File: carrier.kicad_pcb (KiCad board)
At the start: 4 copper layers, 20.3 x 68.6 mm, 52 parts, among them J1 Conn_02x06_Odd_Even, J10 Conn_01x02, J11 Conn_01x02, J12 AudioJack3_SwitchTR, J2 Conn_01x26, J3 Conn_01x26, J4 TYPE-C-31-M-12, J5 Conn_01x02, J6 Conn_01x02, J7 Conn_01x02, J8 Conn_01x02, J9 Conn_01x02, U1 CARAVEL, U2 W25Q128JVS, U3 LP5907MFX-3.3, U4 LP5907MFX-1.8, U5 LP5907MFX-1.8, U6 LP5907MFX-3.3, U7 TPD2E001DRSR, U8 OPA340NA, U9 OPA340NA, X1 SG-5032CAN

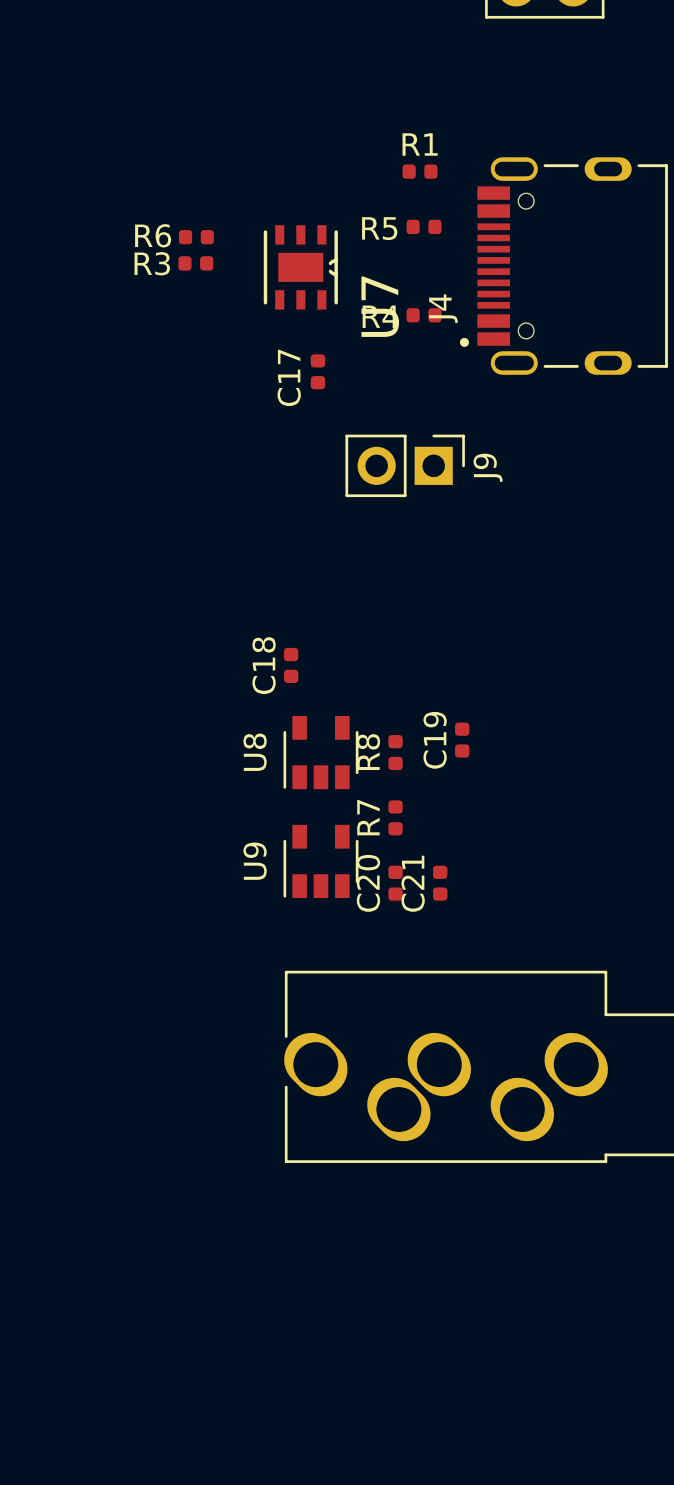
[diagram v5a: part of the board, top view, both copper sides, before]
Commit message: Add GND hook test point
Might want to add more test points for various things.
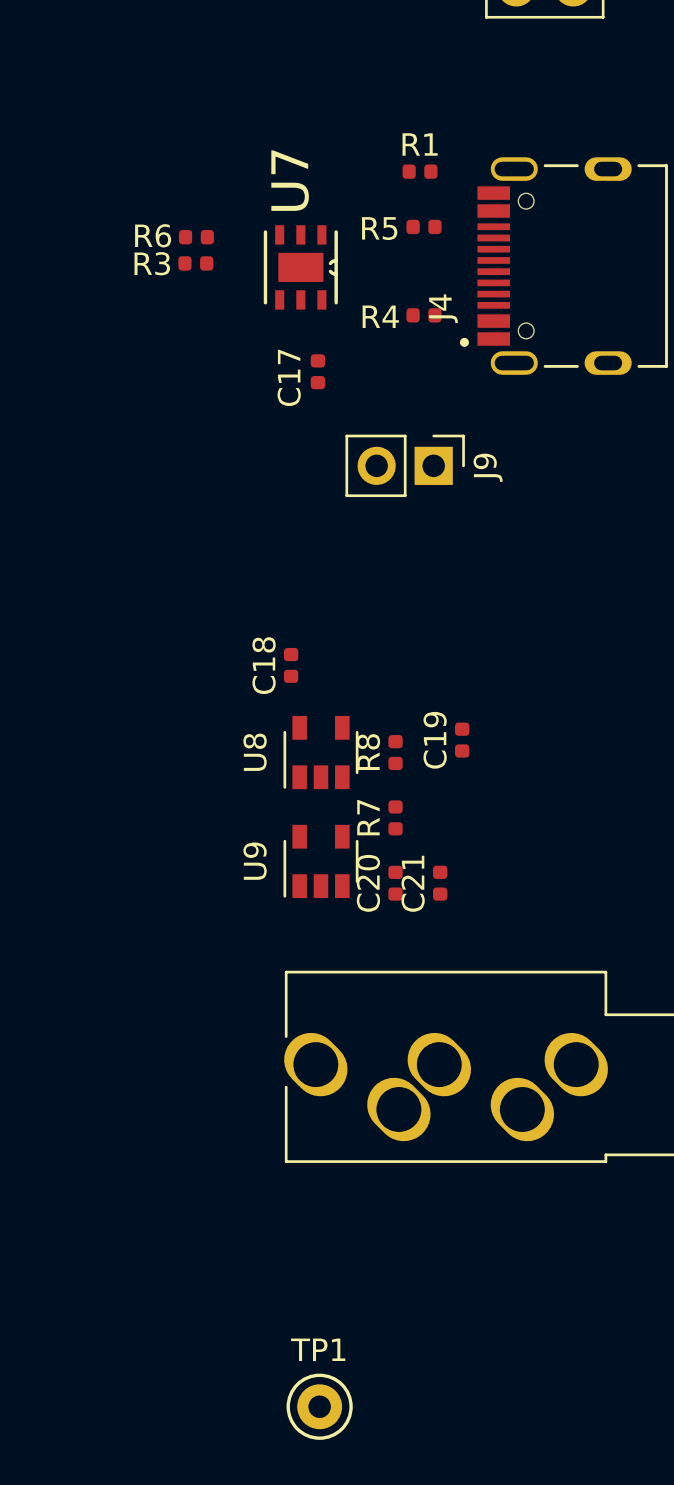
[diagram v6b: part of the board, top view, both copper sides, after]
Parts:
- added TP1: TestPoint, TestPoint:TestPoint_Keystone_5000-5004_Miniature, F.Cu at (114.3, 123.2)
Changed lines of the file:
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@@
     (property "Sheetname" "")
     (attr through_hole)
-    (fp_text reference "U7" (at 1.753155 -3.582515 -90) (layer "F.SilkS")
+    (fp_text reference "U7" (at -3.8608 0.4318 -90) (layer "F.SilkS")
       (effects (font (size 1.640512 1.640512) (thickness 0.015)))
     )
@@
       (net 89 "pcm_audio_2") (pintype "passive"))
     (model "${KISYS3DMOD}/Resistor_SMD.3dshapes/R_0402_1005Metric.wrl"
+      (offset (xyz 0 0 0))
+      (scale (xyz 1 1 1))
+      (rotate (xyz 0 0 0))
+    )
+  )
+  (footprint "TestPoint:TestPoint_Keystone_5000-5004_Miniature" (layer "F.Cu")
+    (at 114.3 123.19)
+    (descr "Keystone Miniature THM Test Point 5000-5004, http://www.keyelco.com/product-pdf.cfm?p=1309")
+    (tags "Through Hole Mount Test Points")
+    (property "Sheetfile" "carrier.kicad_sch")
+    (property "Sheetname" "")
+    (attr through_hole)
+    (fp_text reference "TP1" (at 0 -2.5) (layer "F.SilkS")
+      (effects (font (size 1 1) (thickness 0.15)))
+    )
+    (fp_text value "TestPoint" (at 0 2.5) (layer "F.Fab")
+      (effects (font (size 1 1) (thickness 0.15)))
+    )
+    (fp_text user "${REFERENCE}" (at 0 -2.5) (layer "F.Fab")
+      (effects (font (size 1 1) (thickness 0.15)))
+    )
+    (fp_circle (center 0 0) (end 1.4 0) (layer "F.SilkS") (width 0.15) (fill none))
+    (fp_circle (center 0 0) (end 1.65 0) (layer "F.CrtYd") (width 0.05) (fill none))
+    (fp_line (start -0.75 0.25) (end -0.75 -0.25) (layer "F.Fab") (width 0.15))
+    (fp_line (start 0.75 -0.25) (end 0.75 0.25) (layer "F.Fab") (width 0.15))
+    (fp_line (start -0.75 -0.25) (end 0.75 -0.25) (layer "F.Fab") (width 0.15))
+    (fp_line (start 0.75 0.25) (end -0.75 0.25) (layer "F.Fab") (width 0.15))
+    (fp_circle (center 0 0) (end 1.25 0) (layer "F.Fab") (width 0.15) (fill none))
+    (pad "1" thru_hole circle locked (at 0 0) (size 2 2) (drill 1) (layers *.Cu *.Mask)
+      (net 3 "GND") (pinfunction "1") (pintype "passive"))
+    (model "${KISYS3DMOD}/TestPoint.3dshapes/TestPoint_Keystone_5000-5004_Miniature.wrl"
       (offset (xyz 0 0 0))
       (scale (xyz 1 1 1))
@@
       (effects (font (size 1 1) (thickness 0.15)))
     )
+    (fp_line (start 4.47 2.6) (end -4.47 2.6) (layer "F.SilkS") (width 0.127))
+    (fp_line (start 4.47 1.37) (end 4.47 2.6) (layer "F.SilkS") (width 0.127))
+    (fp_line (start -4.47 -2.81) (end -4.47 -1.37) (layer "F.SilkS") (width 0.127))
     (fp_line (start -4.47 2.6) (end -4.47 1.37) (layer "F.SilkS") (width 0.127))
     (fp_line (start 4.47 -2.81) (end 4.47 -1.37) (layer "F.SilkS") (width 0.127))
-    (fp_line (start -4.47 -2.81) (end -4.47 -1.37) (layer "F.SilkS") (width 0.127))
-    (fp_line (start 4.47 1.37) (end 4.47 2.6) (layer "F.SilkS") (width 0.127))
-    (fp_line (start 4.47 2.6) (end -4.47 2.6) (layer "F.SilkS") (width 0.127))
     (fp_circle (center -3.4 -6.4) (end -3.3 -6.4) (layer "F.SilkS") (width 0.2) (fill none))
     (fp_line (start 5.095 2.85) (end 5.095 -6.07) (layer "F.CrtYd") (width 0.05))
     (fp_line (start -5.095 -6.07) (end -5.095 2.85) (layer "F.CrtYd") (width 0.05))
+    (fp_line (start -5.095 2.85) (end 5.095 2.85) (layer "F.CrtYd") (width 0.05))
     (fp_line (start 5.095 -6.07) (end -5.095 -6.07) (layer "F.CrtYd") (width 0.05))
-    (fp_line (start -5.095 2.85) (end 5.095 2.85) (layer "F.CrtYd") (width 0.05))
+    (fp_line (start -4.47 2.6) (end 4.47 2.6) (layer "F.Fab") (width 0.127))
     (fp_line (start 4.47 2.6) (end 4.47 -4.7) (layer "F.Fab") (width 0.127))
     (fp_line (start 4.47 -4.7) (end -4.47 -4.7) (layer "F.Fab") (width 0.127))
-    (fp_line (start -4.47 2.6) (end 4.47 2.6) (layer "F.Fab") (width 0.127))
     (fp_line (start -4.47 -4.7) (end -4.47 2.6) (layer "F.Fab") (width 0.127))
     (fp_circle (center -3.4 -6.4) (end -3.3 -6.4) (layer "F.Fab") (width 0.2) (fill none))
+    (pad "" np_thru_hole circle locked (at -2.89 -3.65 90) (size 0.7 0.7) (drill 0.7) (layers *.Cu *.Mask))
     (pad "" np_thru_hole circle locked (at 2.89 -3.65 90) (size 0.7 0.7) (drill 0.7) (layers *.Cu *.Mask))
-    (pad "" np_thru_hole circle locked (at -2.89 -3.65 90) (size 0.7 0.7) (drill 0.7) (layers *.Cu *.Mask))
     (pad "A1B12" smd rect locked (at -3.25 -5.095 90) (size 0.6 1.45) (layers "F.Cu" "F.Paste" "F.Mask")
       (net 3 "GND") (pinfunction "GND") (pintype "power_in"))
@@
     (fp_line (start -0.5 0.25) (end -0.5 -0.25) (layer "F.Fab") (width 0.1))
     (pad "1" smd roundrect locked (at -0.485 0 90) (size 0.59 0.64) (layers "F.Cu" "F.Paste" "F.Mask") (roundrect_rratio 0.25)
-      (net 82 "Net-(C19-Pad1)"))
+      (net 82 "Net-(C19-Pad1)") (pintype "passive"))
     (pad "2" smd roundrect locked (at 0.485 0 90) (size 0.59 0.64) (layers "F.Cu" "F.Paste" "F.Mask") (roundrect_rratio 0.25)
-      (net 3 "GND"))
+      (net 3 "GND") (pintype "passive"))
     (model "${KISYS3DMOD}/Capacitor_SMD.3dshapes/C_0402_1005Metric.wrl"
       (offset (xyz 0 0 0))

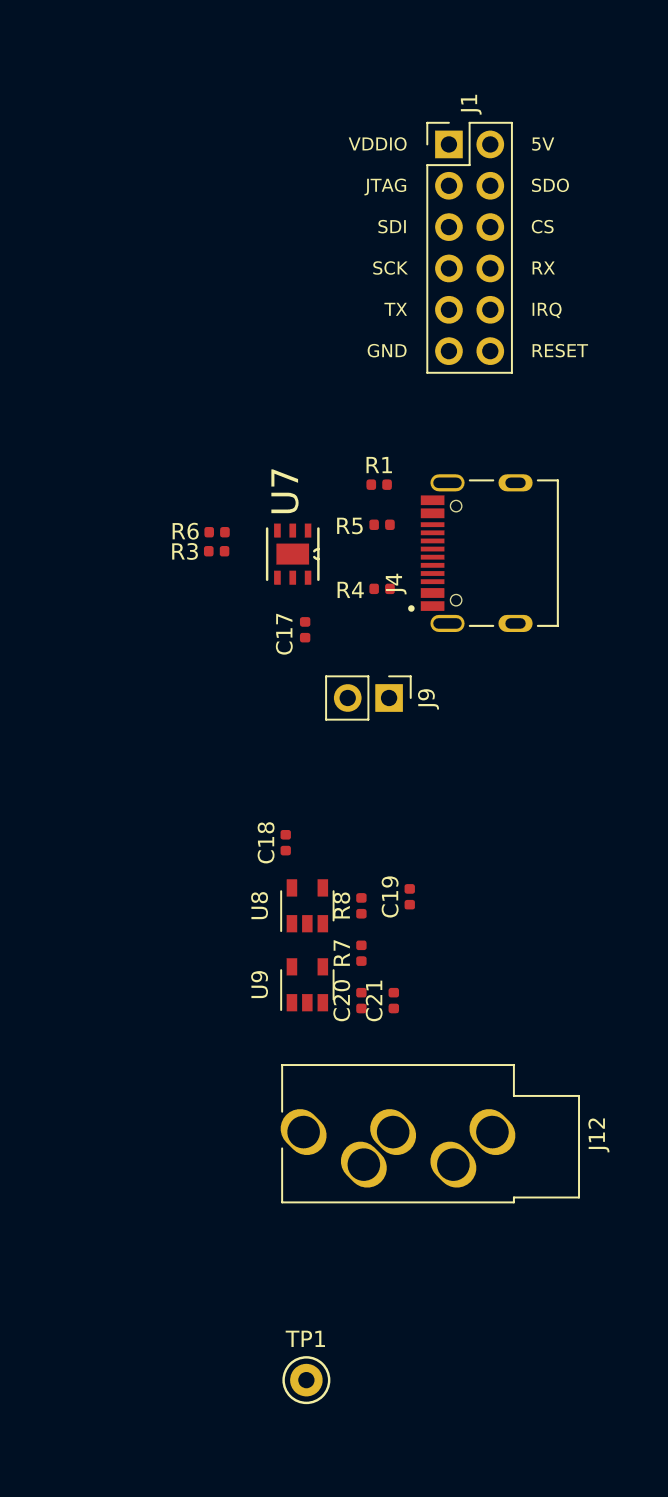
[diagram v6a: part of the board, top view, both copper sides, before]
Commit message: Add video connector
May want to use PMOD specific connector numbering to avoid confusion.
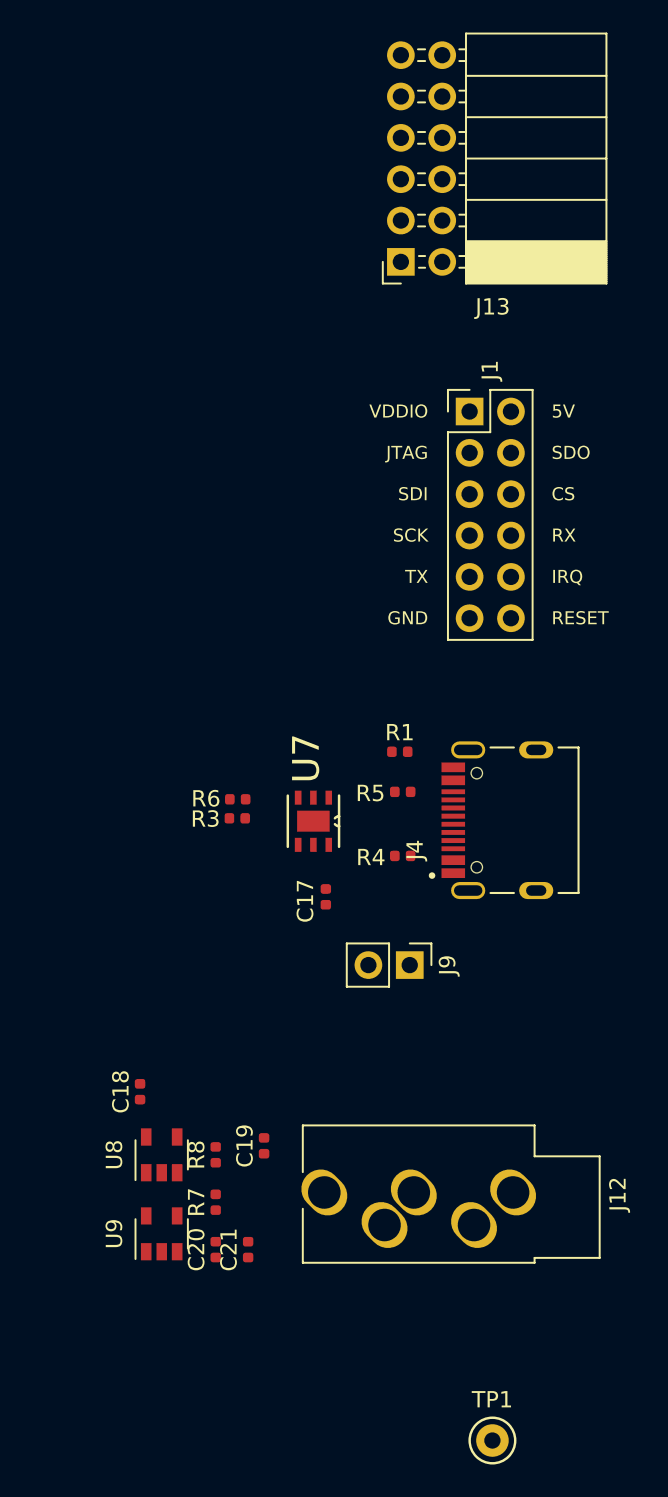
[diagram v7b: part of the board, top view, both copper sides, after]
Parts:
- added J13: Conn_02x06_Odd_Even, Connector_PinSocket_2.54mm:PinSocket_2x06_P2.54mm_Horizontal, F.Cu at (120.1, 54.5)
- moved R7 17.7 mm to (108.7, 112.3)
- moved C18 17.7 mm to (104.1, 105.5)
- moved C19 17.7 mm to (111.7, 108.8)
- moved C20 17.7 mm to (108.7, 115.2)
- moved C21 17.7 mm to (110.7, 115.2)
- moved R8 17.7 mm to (108.7, 109.3)
- moved U8 17.7 mm to (105.4, 109.3)
- moved U9 17.7 mm to (105.4, 114.2)
- moved R1 16.5 mm to (120.0, 84.6)
- moved U7 16.5 mm to (114.7, 88.9)
- moved J4 16.5 mm to (128.4, 88.8)
- moved J1 16.5 mm to (124.3, 63.7)
- moved J9 16.5 mm to (120.7, 97.7)
- moved R3 16.5 mm to (110.1, 88.7)
- moved C17 16.5 mm to (115.5, 93.5)
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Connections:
- J2 pad 24: mprj_io[17] -> unconnected-(J2-Pad24)
- J2 pad 25: mprj_io[18] -> unconnected-(J2-Pad25)
- J3 pad 19: mprj_io[26] -> unconnected-(J3-Pad19)
- J3 pad 20: mprj_io[25] -> unconnected-(J3-Pad20)
- J3 pad 21: mprj_io[24] -> unconnected-(J3-Pad21)
- J3 pad 22: mprj_io[23] -> unconnected-(J3-Pad22)
- J3 pad 23: mprj_io[22] -> unconnected-(J3-Pad23)
- J3 pad 24: mprj_io[21] -> unconnected-(J3-Pad24)
- J3 pad 25: mprj_io[20] -> unconnected-(J3-Pad25)
- J3 pad 26: mprj_io[19] -> unconnected-(J3-Pad26)
- U1 pad A1: mprj_io[23] -> video_r
- U1 pad A3: mprj_io[25] -> video_b
- U1 pad B1: mprj_io[21] -> video_hsync
- U1 pad B2: mprj_io[22] -> video_vsync
- U1 pad B4: mprj_io[26] -> video_i
- U1 pad C1: mprj_io[19] -> video_clk
- U1 pad C2: mprj_io[20] -> video_de
- U1 pad C3: mprj_io[24] -> video_g

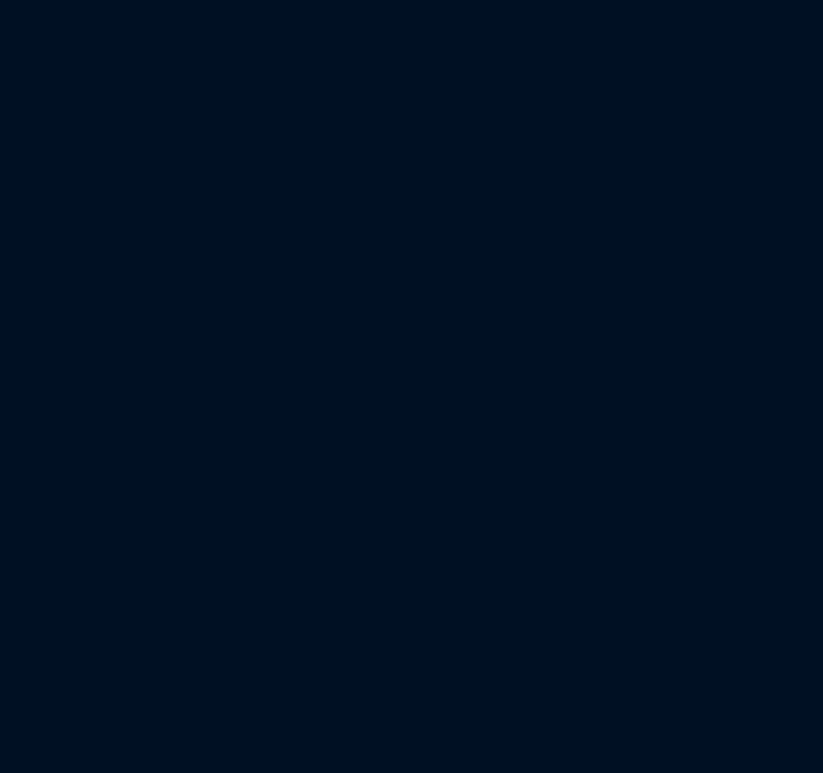
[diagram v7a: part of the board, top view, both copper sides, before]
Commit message: Add some buttons
May want to consider adding ESD clamps to buttons.
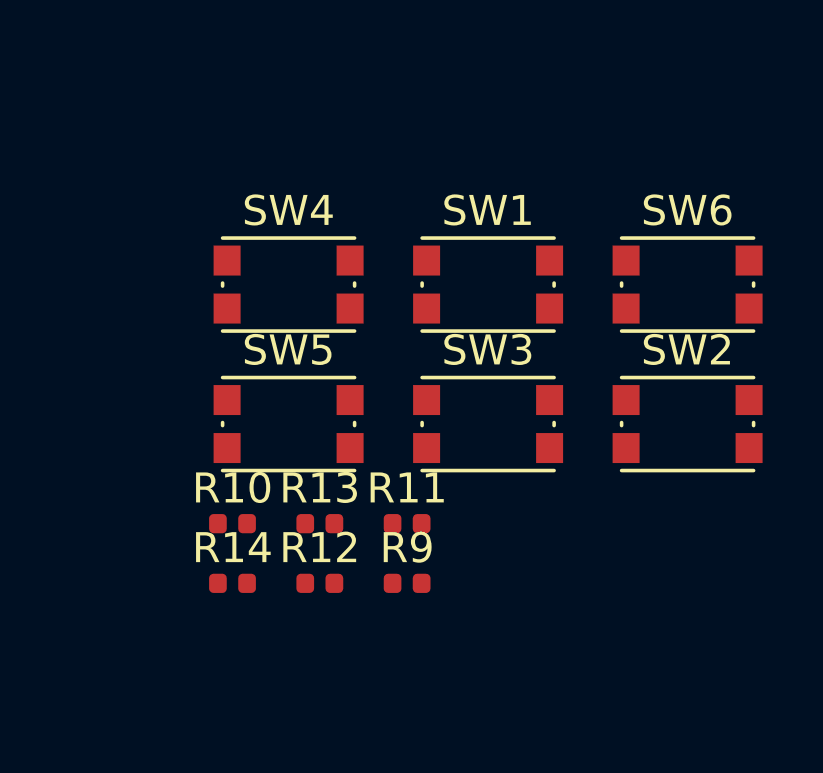
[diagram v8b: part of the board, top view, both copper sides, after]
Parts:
- added R10: 10k Ohm, Resistor_SMD:R_0402_1005Metric, F.Cu at (149.1, 100.9)
- added R11: 10k Ohm, Resistor_SMD:R_0402_1005Metric, F.Cu at (154.9, 100.9)
- added R12: 10k Ohm, Resistor_SMD:R_0402_1005Metric, F.Cu at (152.0, 102.9)
- added R13: 10k Ohm, Resistor_SMD:R_0402_1005Metric, F.Cu at (152.0, 100.9)
- added R14: 10k Ohm, Resistor_SMD:R_0402_1005Metric, F.Cu at (149.1, 102.9)
- added R9: 10k Ohm, Resistor_SMD:R_0402_1005Metric, F.Cu at (154.9, 102.9)
- added SW1: SW_Push, Button_Switch_SMD:SW_Push_1P1T_NO_CK_KMR2, F.Cu at (157.6, 92.9)
- added SW2: SW_Push, Button_Switch_SMD:SW_Push_1P1T_NO_CK_KMR2, F.Cu at (164.3, 97.6)
- added SW3: SW_Push, Button_Switch_SMD:SW_Push_1P1T_NO_CK_KMR2, F.Cu at (157.6, 97.6)
- added SW4: SW_Push, Button_Switch_SMD:SW_Push_1P1T_NO_CK_KMR2, F.Cu at (151.0, 92.9)
- added SW5: SW_Push, Button_Switch_SMD:SW_Push_1P1T_NO_CK_KMR2, F.Cu at (151.0, 97.6)
- added SW6: SW_Push, Button_Switch_SMD:SW_Push_1P1T_NO_CK_KMR2, F.Cu at (164.3, 92.9)
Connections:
- J2 pad 18: mprj_io[11] -> unconnected-(J2-Pad18)
- J2 pad 19: mprj_io[12] -> unconnected-(J2-Pad19)
- J2 pad 20: mprj_io[13] -> unconnected-(J2-Pad20)
